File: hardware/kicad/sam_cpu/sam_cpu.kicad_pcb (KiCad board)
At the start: 2 copper layers, 142 x 231.8 mm, 465 parts, among them J1 J1 SWITCH COLUMNS, J10 J10 SPEAKERS, J11 J11 POWER, J12 J12 SWITCH ROWS, J13 J13 DEDICATED, J17 EXT 5V, J18 J18 GI DIMMER, J19 USB-C (to Pi), J2 J2 DEDICATED, J20 SWD, J21 Raspberry Pi 40-pin, J22 J22 STEREO, J23 EXT 12V, J24 J24 SUBWOOFER, J25 J25 HUB75 PANEL A, J26 J26 HUB75 PANEL B, J3 J3 DEDICATED, J5 J5 DMD, J6 J6 SWITCH ROWS, J9 J9 IO BUS, Q1 AO3401A, Q11 MMBT3904, Q12 MMBT3904, Q13 MMBT3904, Q14 MMBT3904, Q15 MMBT3904, Q16 MMBT3904, Q17 MMBT3904, Q18 MMBT3904, Q2 AO3401A, Q3 2N7002, Q4 2N7002, SW1 RESET, SW2 BOOTSEL, SW3 DIP x8, U1 LTC4412, U10 LM339, U11 LM339, U14 74HC165, U15 74HC165, U16 74HC165, U17 74HC165, U18 74HC165, U19 74HC165, U2 LTC4412, U20 74HC595, U21 74HCT245, U22 PCM5102A, U23 TDA7297, U24 TDA7297, U25 DS3231MZ, U26 OPA1678, U27 74AHCT245, U28 74AHCT245, U29 74AHCT245, U3 NCP1117-3.3, U30 74HC165, U31 74HC595, U4 RP2354B, U5 TPS3808G33, U6 SN74LVC8T245, U7 74AHCT541, U8 LM339, U9 LM339, Y1 12MHz

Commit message: Layout: 4 copper layers with inner GND and +3V3 planes (pending Vincent's OK)
2-layer autoroutes stalled at 39-170 open connections. In1.Cu is a GND
plane and In2.Cu a +3V3 plane; F.Cu and B.Cu stay the signal layers.
Easy to revert with SetCopperLayerCount(2) if Vincent prefers 2 layers.

Co-Authored-By: Claude Opus 5.5 (1M context) <noreply@anthropic.com>
Claude-Session: https://claude.ai/code/session_01ExuDVoDDDHhVWjb8EwVzYb
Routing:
- added copper zone on In2.Cu, net +3V3
- added copper zone on In1.Cu, net GND
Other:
- copper layers 2 -> 4
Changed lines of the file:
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@@
 	(layers
 		(0 "F.Cu" signal)
+		(4 "In1.Cu" power)
+		(6 "In2.Cu" power)
 		(2 "B.Cu" signal)
 		(9 "F.Adhes" user "F.Adhesive")
@@
 		(hatch edge 0.5)
 		(connect_pads
+			(clearance 0.25)
+		)
+		(min_thickness 0.2)
+		(fill
+			(thermal_gap 0.3)
+			(thermal_bridge_width 0.4)
+			(island_removal_mode 0)
+		)
+		(polygon
+			(pts
+				(xy 150.65 184) (xy 172 184) (xy 172 261.76) (xy 30 261.76) (xy 30 30) (xy 150.65 30)
+			)
+		)
+	)
+	(zone
+		(net "GND")
+		(layer "In1.Cu")
+		(name "GND_PLANE")
+		(hatch edge 0.5)
+		(connect_pads
+			(clearance 0.25)
+		)
+		(min_thickness 0.2)
+		(fill
+			(thermal_gap 0.3)
+			(thermal_bridge_width 0.4)
+			(island_removal_mode 0)
+		)
+		(polygon
+			(pts
+				(xy 150.65 184) (xy 172 184) (xy 172 261.76) (xy 30 261.76) (xy 30 30) (xy 150.65 30)
+			)
+		)
+	)
+	(zone
+		(net "+3V3")
+		(layer "In2.Cu")
+		(name "3V3_PLANE")
+		(hatch edge 0.5)
+		(connect_pads

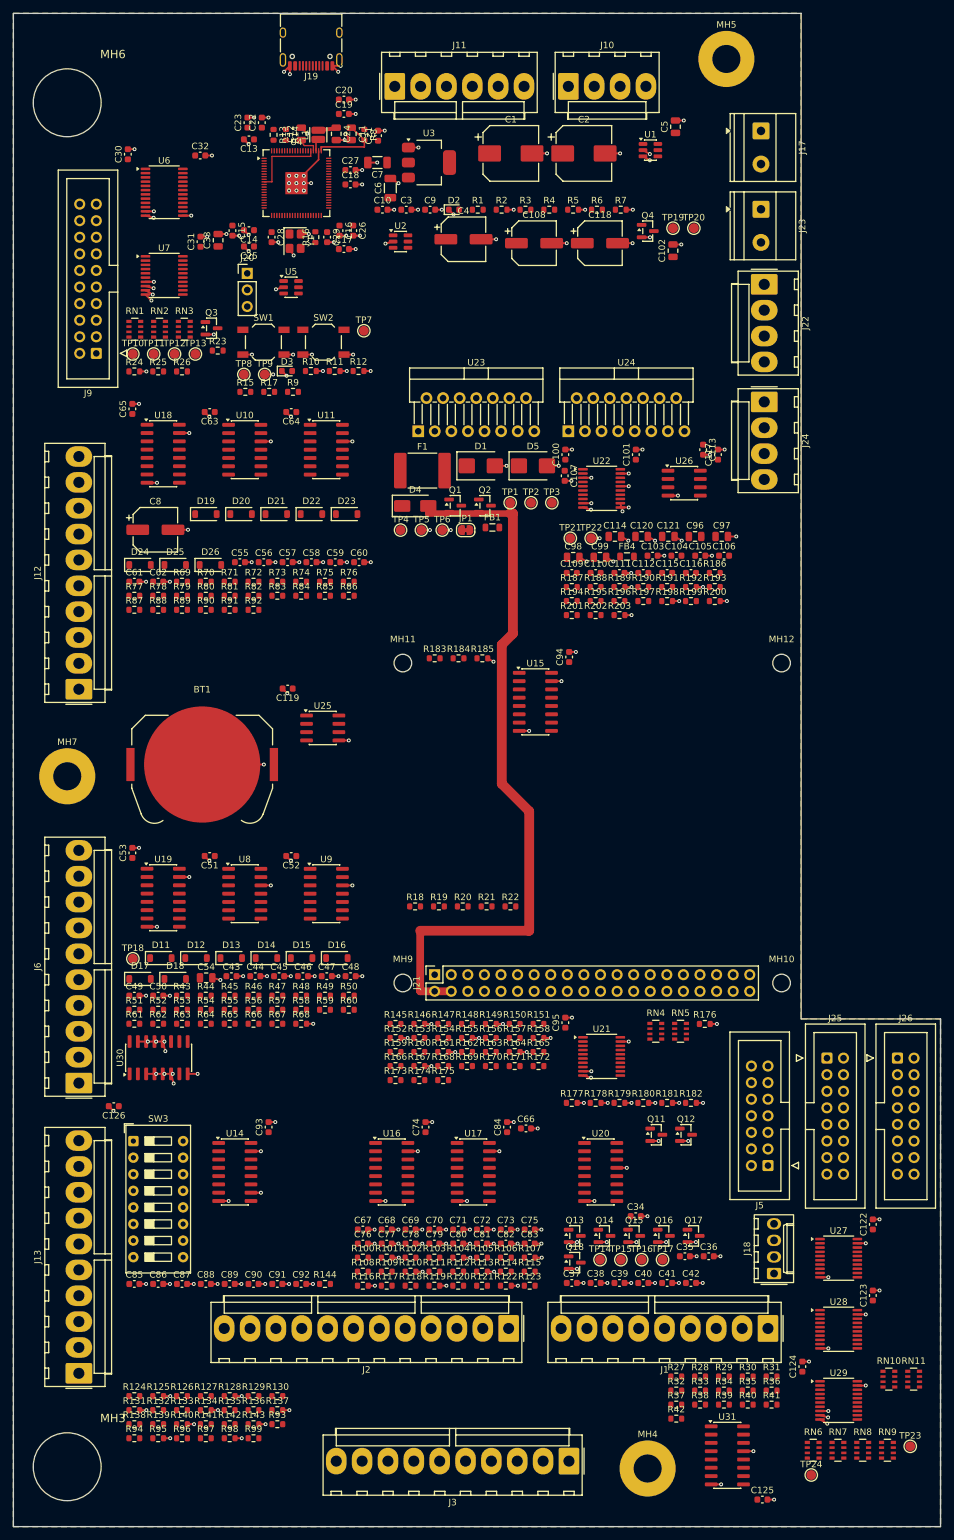
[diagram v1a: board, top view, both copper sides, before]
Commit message: Layout: via to the +3V3 plane per SMD +3V3 pad
tools/changes/c09_plane_fanout.py (c07 generalised to any plane net, stub no
wider than the pad): 89 of 91 +3V3 pads now drop to In2.Cu.

Co-Authored-By: Claude Opus 5.5 (1M context) <noreply@anthropic.com>
Claude-Session: https://claude.ai/code/session_01ExuDVoDDDHhVWjb8EwVzYb
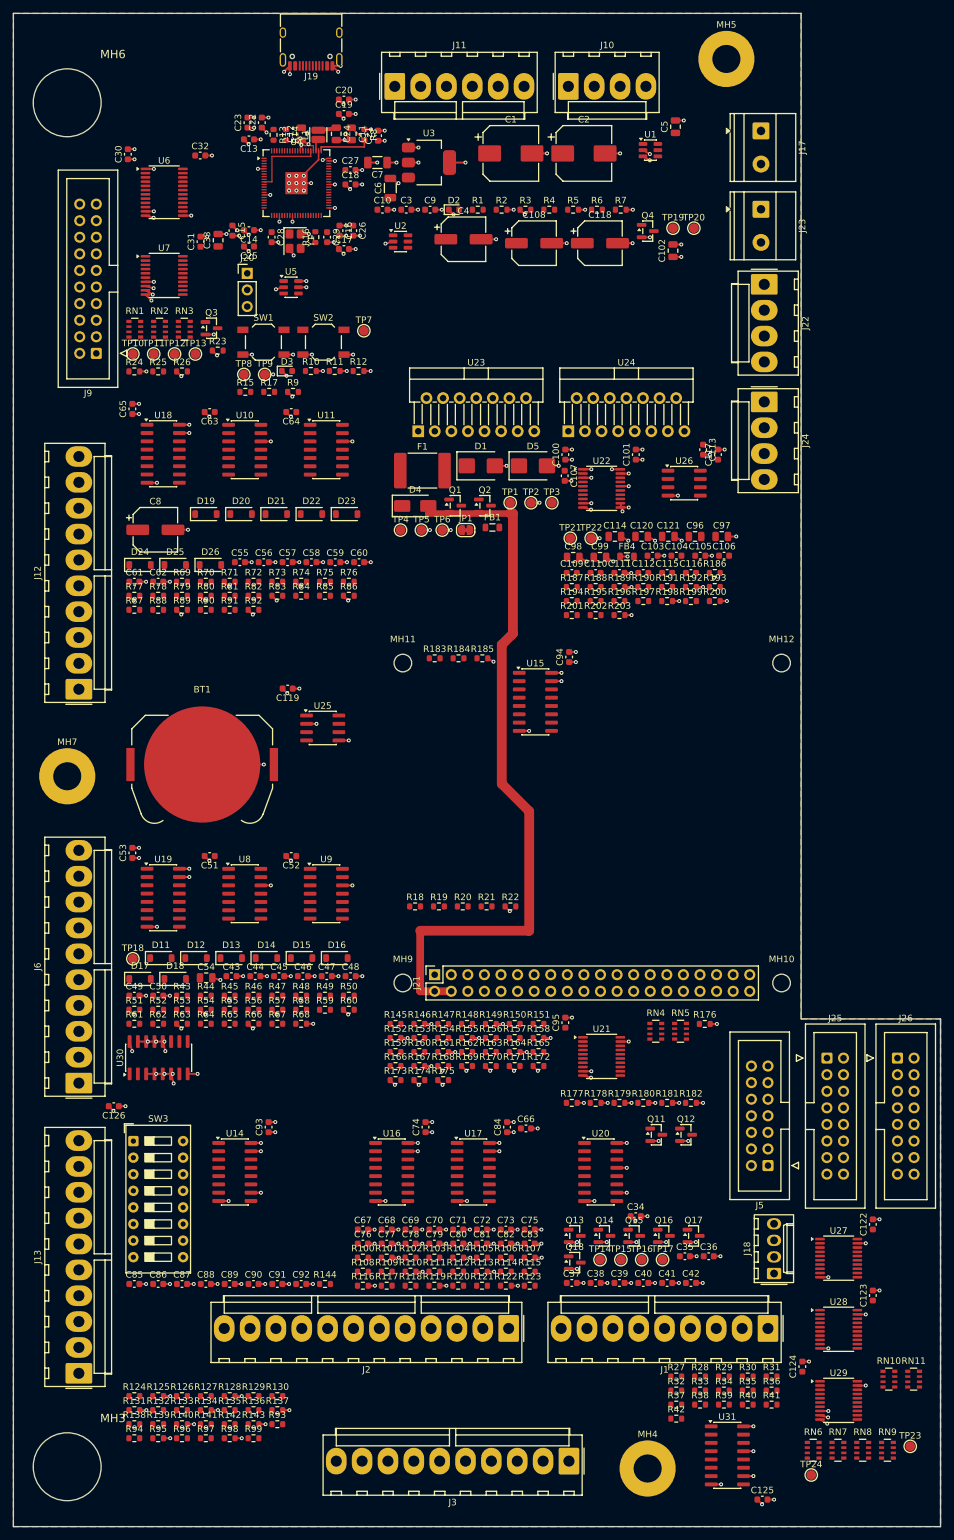
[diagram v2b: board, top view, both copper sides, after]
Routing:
- net +3V3: track 2.63 -> 104.5 mm, vias 0 -> 89

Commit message: Layout: autorouted 4-layer board, 35 connections left open
Freerouting 2.5 (10 passes, GND and +3V3 on the inner planes) routed all but
35 connections, mostly RP2354B escapes and the DMD buffers. GND pours on
F.Cu/B.Cu filled. Minimum track width set to 0.1 mm for the autorouter's
pad neck-downs (JLCPCB capability).

Co-Authored-By: Claude Opus 5.5 (1M context) <noreply@anthropic.com>
Claude-Session: https://claude.ai/code/session_01ExuDVoDDDHhVWjb8EwVzYb
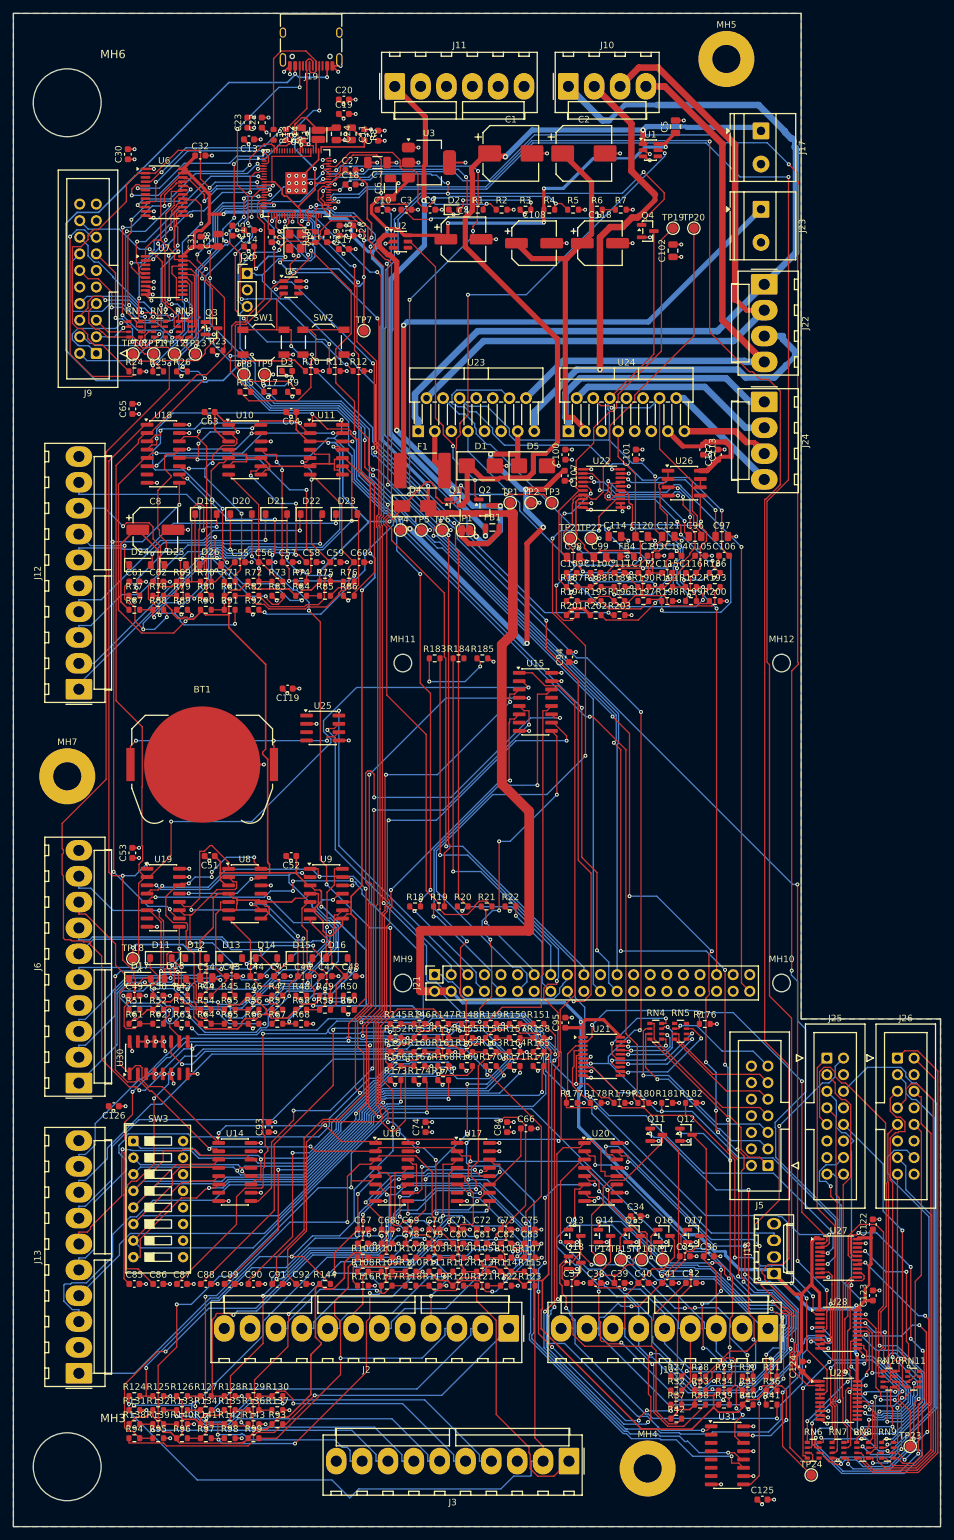
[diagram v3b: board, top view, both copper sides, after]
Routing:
- net +4V5: track 0.00 -> 584.2 mm, vias 0 -> 8
- net SW_CLK: track 0.00 -> 413.2 mm, vias 0 -> 14
- net SW_LOAD_N: track 0.00 -> 402.3 mm, vias 0 -> 7
- net +5V: track 112.8 -> 458.1 mm, vias 0 -> 10
- net DMD_LAT: track 0.00 -> 306.9 mm, vias 0 -> 6
- net DMD_OE: track 0.00 -> 273.0 mm, vias 0 -> 2
- net SW_DATA: track 0.00 -> 269.5 mm, vias 0 -> 7
- net DMD_D9: track 0.00 -> 269.5 mm, vias 0 -> 6
- net DMD_A: track 0.00 -> 269.4 mm, vias 0 -> 4
- net STB_DATA: track 0.00 -> 243.3 mm, vias 0 -> 16
- net DMD_D1: track 0.00 -> 240.8 mm, vias 0 -> 6
- net DMD_D6: track 0.00 -> 230.5 mm, vias 0 -> 6
- net DMD_D5: track 0.00 -> 218.1 mm, vias 0 -> 8
- net LED_STATUS: track 0.00 -> 213.6 mm, vias 0 -> 14
- net DMD_D10: track 0.00 -> 205.5 mm, vias 0 -> 6
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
